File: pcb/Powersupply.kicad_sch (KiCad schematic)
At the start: 0 parts

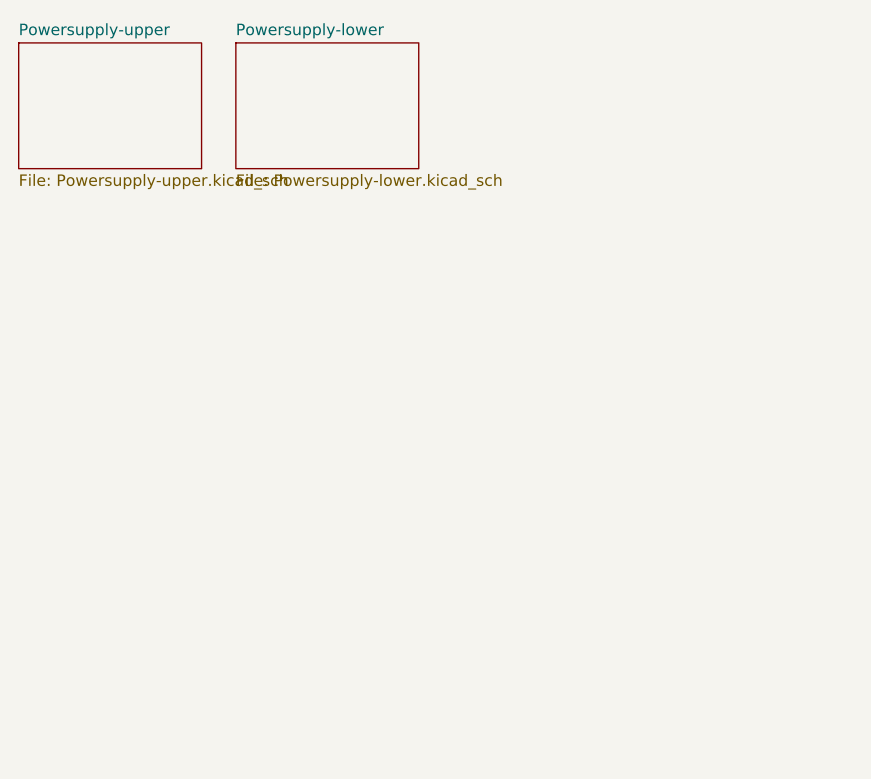
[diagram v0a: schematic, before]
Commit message: pcb: connect upper and lower
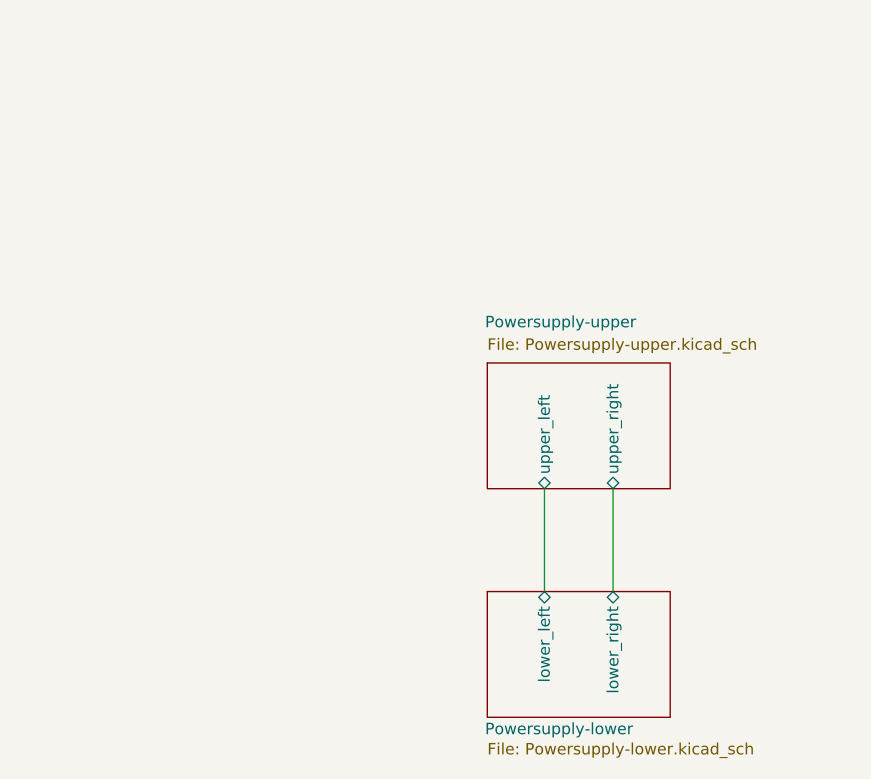
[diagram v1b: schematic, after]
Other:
- sheet Powersupply-lower ports: added lower_left, lower_right; removed none
- sheet Powersupply-upper ports: added upper_left, upper_right; removed none
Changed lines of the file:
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@@
 	(generator_version "10.0")
 	(paper "A4")
+	(wire
+		(pts
+			(xy 99.06 85.09) (xy 99.06 73.66)
+		)
+		(stroke
+			(width 0)
+			(type default)
+		)
+	)
+	(wire
+		(pts
+			(xy 91.44 85.09) (xy 91.44 73.66)
+		)
+		(stroke
+			(width 0)
+			(type default)
+		)
+	)
 	(sheet
-		(at 33.02 24.13)
+		(at 85.09 59.69)
 		(size 20.32 13.97)
 		(exclude_from_sim no)
@@
 		(on_board yes)
 		(dnp no)
-		(fields_autoplaced yes)
 		(stroke
 			(width 0.1524)
@@
 		)
 		(property "Sheetname" "Powersupply-upper"
-			(at 33.02 23.4184 0)
+			(at 84.836 55.88 0)
 			(show_name no)
 			(do_not_autoplace no)
@@
 		)
 		(property "Sheetfile" "Powersupply-upper.kicad_sch"
-			(at 33.02 38.6846 0)
+			(at 85.09 56.896 0)
 			(show_name no)
 			(do_not_autoplace no)
@@
 				)
 				(justify left top)
+			)
+		)
+		(pin "upper_left" bidirectional
+			(at 91.44 73.66 270)
+			(effects
+				(font
+					(size 1.27 1.27)
+				)
+				(justify left)
+			)
+		)
+		(pin "upper_right" bidirectional
+			(at 99.06 73.66 270)
+			(effects
+				(font
+					(size 1.27 1.27)
+				)
+				(justify left)
 			)
 		)
@@
 	)
 	(sheet
-		(at 57.15 24.13)
+		(at 85.09 85.09)
 		(size 20.32 13.97)
 		(exclude_from_sim no)
@@
 		(on_board yes)
 		(dnp no)
-		(fields_autoplaced yes)
 		(stroke
 			(width 0.1524)
@@
 		)
 		(property "Sheetname" "Powersupply-lower"
-			(at 57.15 23.4184 0)
+			(at 84.836 101.092 0)
 			(show_name no)
 			(do_not_autoplace no)
@@
 		)
 		(property "Sheetfile" "Powersupply-lower.kicad_sch"
-			(at 57.15 38.6846 0)
+			(at 85.09 101.854 0)
 			(show_name no)
 			(do_not_autoplace no)
@@
 			)
 		)
+		(pin "lower_left" bidirectional
+			(at 91.44 85.09 90)
+			(effects
+				(font
+					(size 1.27 1.27)
+				)
+				(justify right)
+			)
+		)
+		(pin "lower_right" bidirectional
+			(at 99.06 85.09 90)
+			(effects
+				(font
+					(size 1.27 1.27)
+				)
+				(justify right)
+			)
+		)

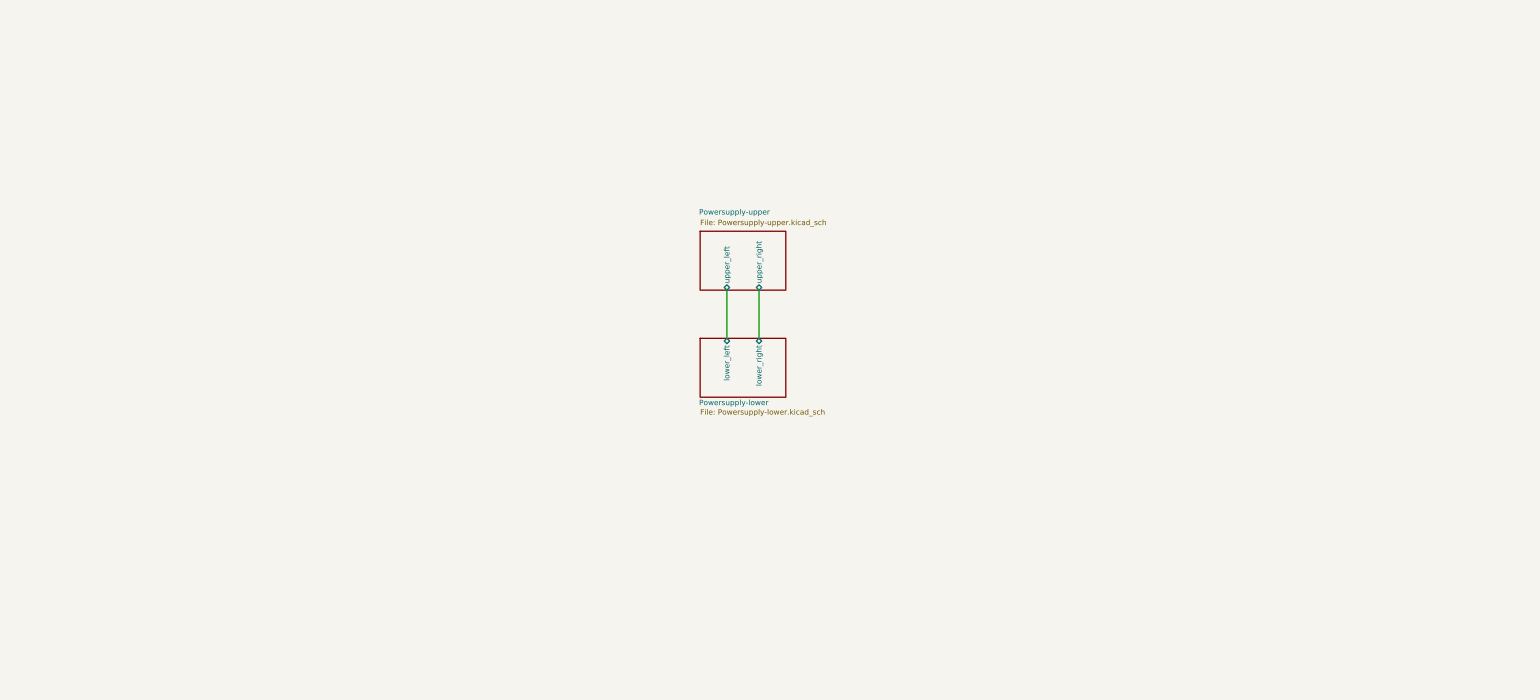
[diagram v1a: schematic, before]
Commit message: pcb: moved powersupply upper & lower to same sheet
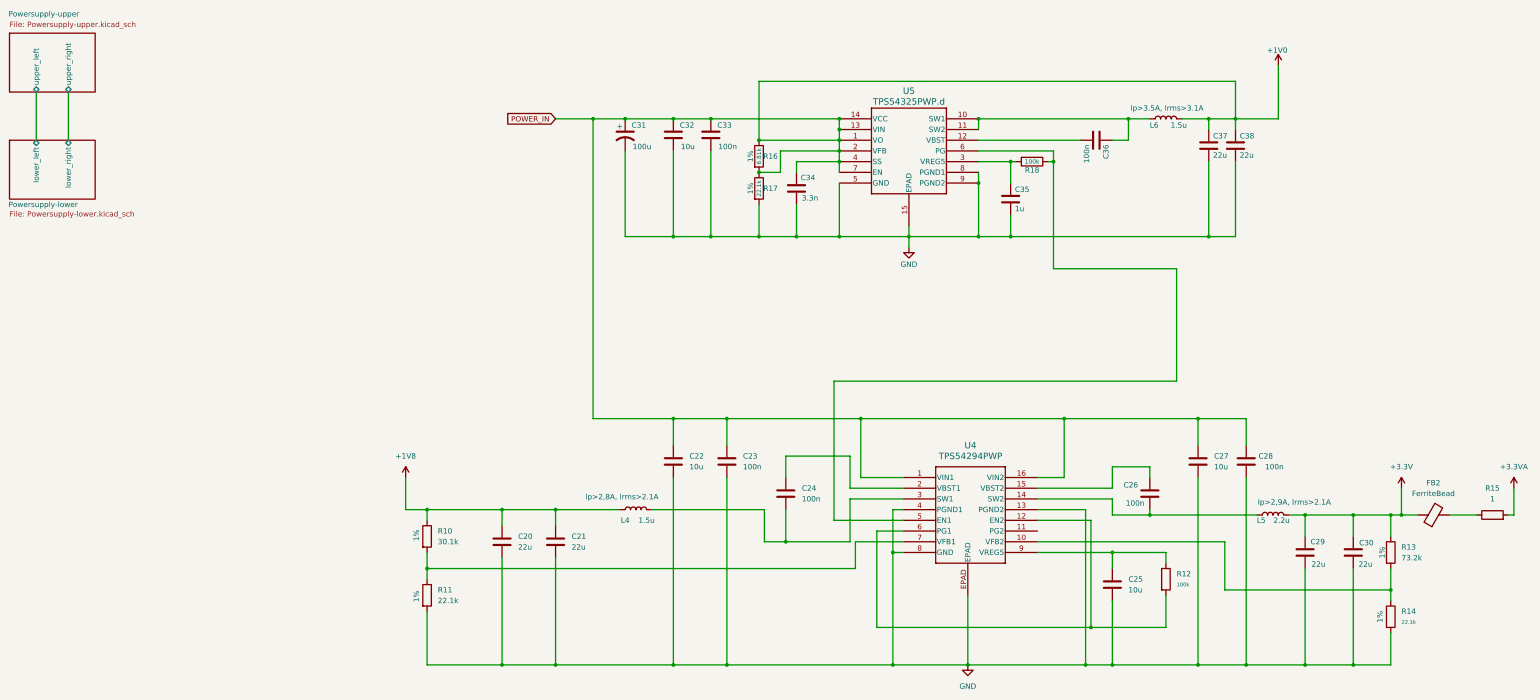
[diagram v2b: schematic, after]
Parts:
- added C20, C21, C29, C30, C37, C38: 22u, symbol Device:C
- added C22, C25, C27, C32: 10u, symbol Device:C
- added C23, C24, C26, C28, C33, C36: 100n, symbol Device:C
- added C31: 100u, symbol Device:C_US
- added C34: 3.3n, symbol Device:C
- added C35: 1u, symbol Device:C
- added FB2: FerriteBead, symbol Device:FerriteBead
- added L4: 1.5u, Relay_THT:Relay_DPDT_Kemet_EC2_NU_DoubleCoil, symbol Device:L
- added L5: 2.2u, Relay_THT:Relay_DPDT_Kemet_EC2_NU_DoubleCoil, symbol Device:L
- added L6: 1.5u, symbol Device:L
- added R10: 30.1k, symbol Device:R
- added R11, R14, R17: 22.1k, symbol Device:R
- added R12, R18: 100k, symbol Device:R
- added R13: 73.2k, symbol Device:R
- added R15: 1, symbol Device:R
- added R16: 6.81k, symbol Device:R
- added U4: TPS54294PWP, PWP16_2P31X2P46, symbol TPS54294PWP:TPS54294PWP
- added U5: TPS54325PWP.d, PWP14_2P31X2P46, symbol TPS54325:TPS54325PWP.d
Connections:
- new net: C36.1, L6.1, U5.10 (SW1), U5.11 (SW2)
- new net: R18.1, U4.5 (EN1), U5.6 (PG)
- new net: C35.1, R18.2, U5.3 (VREG5)
- new net: R13.2, R14.1, U4.10 (VFB2)
- new net: FB2.2, R15.1
- new net: C26.1, U4.15 (VBST2)
- new net: C26.2, L5.1, U4.14 (SW2)
- new net: C24.1, U4.2 (VBST1)
- new net: C24.2, L4.2, U4.3 (SW1)
- new net: C36.2, U5.12 (VBST)
- new net: C25.1, R12.1, U4.9 (VREG5)
- new net: R12.2, U4.12 (EN2), U4.6 (PG1)
- new net: R10.2, R11.1, U4.7 (VFB1)
- new net +1V0: C22.1, C23.1, C27.1, C28.1, C31.1, C32.1, C33.1, C34.1, C37.1, C38.1, L6.2, R16.1, R16.2, R17.1, U4.1 (VIN1), U4.16 (VIN2), U5.1 (VO), U5.13 (VIN), U5.14 (VCC), U5.2 (VFB), U5.4 (SS), U5.7 (EN)
- new net +1V8: C20.1, C21.1, L4.1, R10.1
- new net +3.3V: C29.1, C30.1, FB2.1, L5.2, R13.1
- new net +3.3VA: R15.2
- new net GND: C20.2, C21.2, C22.2, C23.2, C25.2, C27.2, C28.2, C29.2, C30.2, C31.2, C32.2, C33.2, C34.2, C35.2, C37.2, C38.2, R11.2, R14.2, R17.2, U4.13 (PGND2), U4.4 (PGND1), U4.8 (GND), U4.EPAD, U5.15 (EPAD), U5.5 (GND), U5.8 (PGND1), U5.9 (PGND2)
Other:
- note added: "1%"
- note added: "lp>2,8A, lrms>2.1A"
- note added: "lp>2,9A, lrms>2.1A"

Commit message: pcb: changes usbc and add input power
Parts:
- added J7: Conn_02x04_Odd_Even, symbol Connector_Generic:Conn_02x04_Odd_Even
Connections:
- net +1V0: now also J7.1 (Pin_1), J7.7 (Pin_7)
- net +1V8: now also J7.5 (Pin_5)
- net +3.3VA: now also J7.3 (Pin_3)
- net GND: now also J7.2 (Pin_2), J7.4 (Pin_4), J7.6 (Pin_6), J7.8 (Pin_8)
